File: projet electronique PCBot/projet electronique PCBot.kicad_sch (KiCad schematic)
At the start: 0 parts

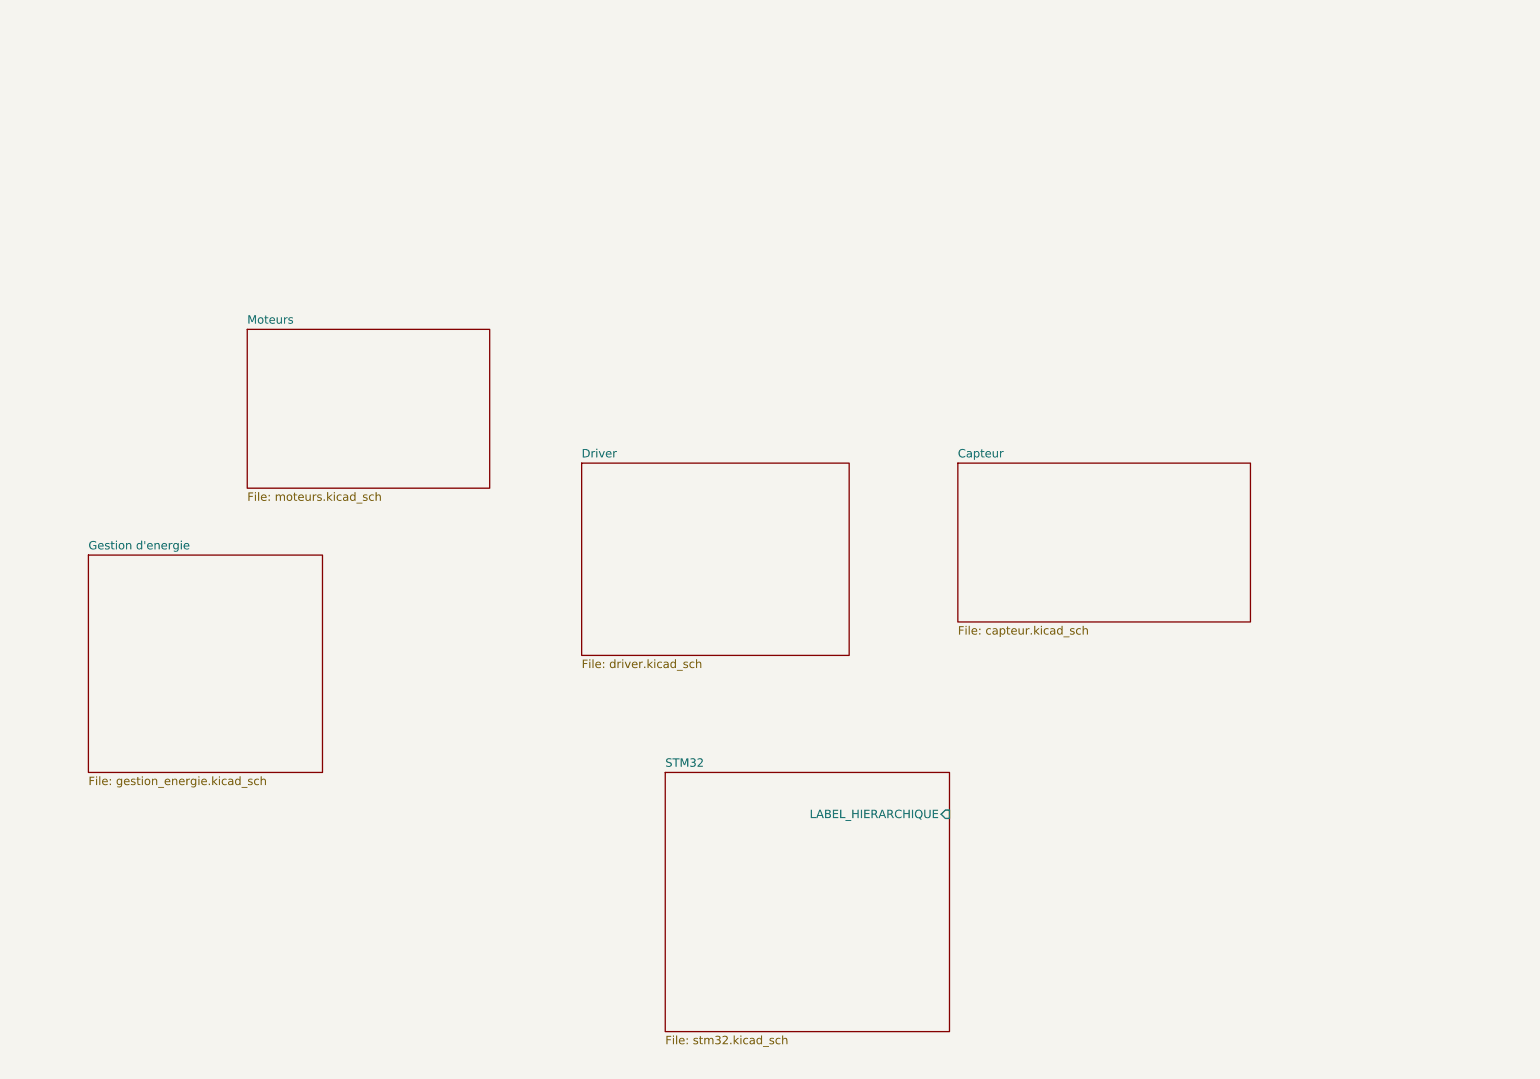
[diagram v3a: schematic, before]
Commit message: Modification des feuilles hiérarchiques et le main
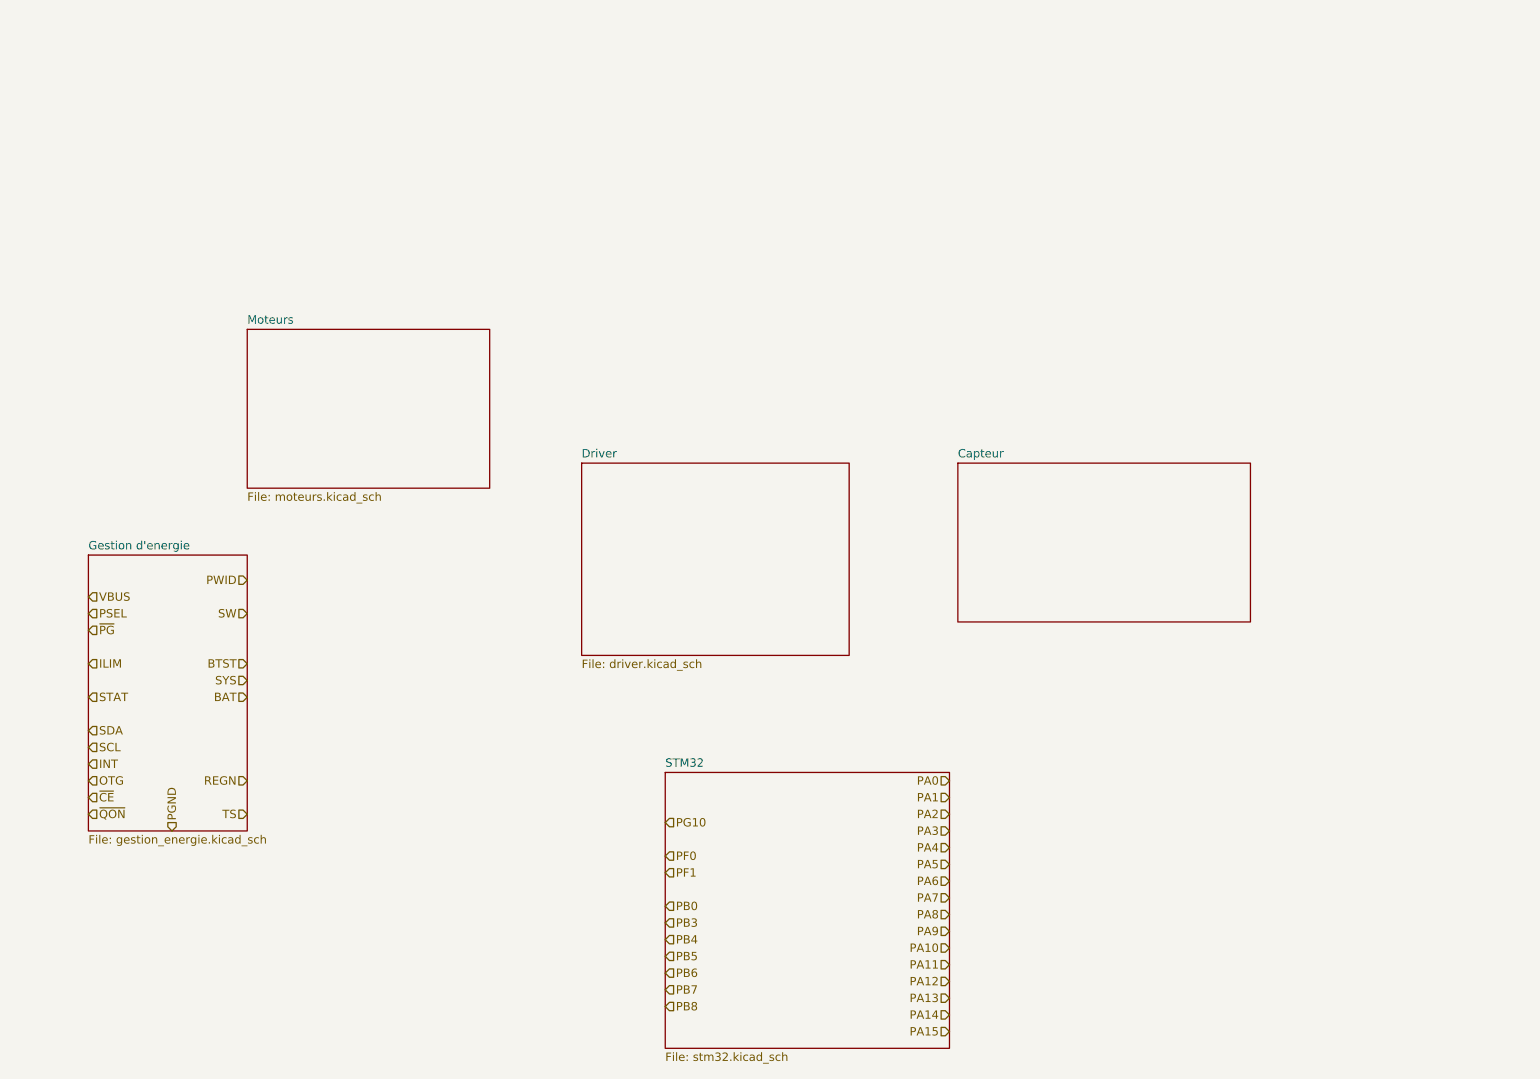
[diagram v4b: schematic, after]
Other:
- sheet STM32 ports: added none; removed LABEL_HIERARCHIQUE
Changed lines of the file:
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@@
     (comment 4 "Sara KABBANI")
   )
-  (sheet (at 115.57 137.16) (size 43.18 39.37) (fields_autoplaced)
+  (hierarchical_label "PF1" (shape input) (at 115.57 152.4 0) (fields_autoplaced)
+    (effects (font (size 1.27 1.27)) (justify left))
+  )
+  (hierarchical_label "PA6" (shape input) (at 158.75 153.67 180) (fields_autoplaced)
+    (effects (font (size 1.27 1.27)) (justify right))
+  )
+  (hierarchical_label "PA8" (shape input) (at 158.75 158.75 180) (fields_autoplaced)
+    (effects (font (size 1.27 1.27)) (justify right))
+  )
+  (hierarchical_label "PA10" (shape input) (at 158.75 163.83 180) (fields_autoplaced)
+    (effects (font (size 1.27 1.27)) (justify right))
+  )
+  (hierarchical_label "TS" (shape input) (at 52.07 143.51 180) (fields_autoplaced)
+    (effects (font (size 1.27 1.27)) (justify right))
+  )
+  (hierarchical_label "OTG" (shape input) (at 27.94 138.43 0) (fields_autoplaced)
+    (effects (font (size 1.27 1.27)) (justify left))
+  )
+  (hierarchical_label "SCL" (shape input) (at 27.94 133.35 0) (fields_autoplaced)
+    (effects (font (size 1.27 1.27)) (justify left))
+  )
+  (hierarchical_label "SDA" (shape input) (at 27.94 130.81 0) (fields_autoplaced)
+    (effects (font (size 1.27 1.27)) (justify left))
+  )
+  (hierarchical_label "STAT" (shape input) (at 27.94 125.73 0) (fields_autoplaced)
+    (effects (font (size 1.27 1.27)) (justify left))
+  )
+  (hierarchical_label "~{CE}" (shape input) (at 27.94 140.97 0) (fields_autoplaced)
+    (effects (font (size 1.27 1.27)) (justify left))
+  )
+  (hierarchical_label "PB3" (shape input) (at 115.57 160.02 0) (fields_autoplaced)
+    (effects (font (size 1.27 1.27)) (justify left))
+  )
+  (hierarchical_label "PA13" (shape input) (at 158.75 171.45 180) (fields_autoplaced)
+    (effects (font (size 1.27 1.27)) (justify right))
+  )
+  (hierarchical_label "PA3" (shape input) (at 158.75 146.05 180) (fields_autoplaced)
+    (effects (font (size 1.27 1.27)) (justify right))
+  )
+  (hierarchical_label "PB8" (shape input) (at 115.57 172.72 0) (fields_autoplaced)
+    (effects (font (size 1.27 1.27)) (justify left))
+  )
+  (hierarchical_label "PA4" (shape input) (at 158.75 148.59 180) (fields_autoplaced)
+    (effects (font (size 1.27 1.27)) (justify right))
+  )
+  (hierarchical_label "~{QON}" (shape input) (at 27.94 143.51 0) (fields_autoplaced)
+    (effects (font (size 1.27 1.27)) (justify left))
+  )
+  (hierarchical_label "PA0" (shape input) (at 158.75 138.43 180) (fields_autoplaced)
+    (effects (font (size 1.27 1.27)) (justify right))
+  )
+  (hierarchical_label "PB6" (shape input) (at 115.57 167.64 0) (fields_autoplaced)
+    (effects (font (size 1.27 1.27)) (justify left))
+  )
+  (hierarchical_label "PB0" (shape input) (at 115.57 157.48 0) (fields_autoplaced)
+    (effects (font (size 1.27 1.27)) (justify left))
+  )
+  (hierarchical_label "PGND" (shape input) (at 40.64 146.05 90) (fields_autoplaced)
+    (effects (font (size 1.27 1.27)) (justify left))
+  )
+  (hierarchical_label "INT" (shape input) (at 27.94 135.89 0) (fields_autoplaced)
+    (effects (font (size 1.27 1.27)) (justify left))
+  )
+  (hierarchical_label "PG10" (shape input) (at 115.57 144.78 0) (fields_autoplaced)
+    (effects (font (size 1.27 1.27)) (justify left))
+  )
+  (hierarchical_label "SW" (shape input) (at 52.07 113.03 180) (fields_autoplaced)
+    (effects (font (size 1.27 1.27)) (justify right))
+  )
+  (hierarchical_label "PA9" (shape input) (at 158.75 161.29 180) (fields_autoplaced)
+    (effects (font (size 1.27 1.27)) (justify right))
+  )
+  (hierarchical_label "~{PG}" (shape input) (at 27.94 115.57 0) (fields_autoplaced)
+    (effects (font (size 1.27 1.27)) (justify left))
+  )
+  (hierarchical_label "BAT" (shape input) (at 52.07 125.73 180) (fields_autoplaced)
+    (effects (font (size 1.27 1.27)) (justify right))
+  )
+  (hierarchical_label "PA12" (shape input) (at 158.75 168.91 180) (fields_autoplaced)
+    (effects (font (size 1.27 1.27)) (justify right))
+  )
+  (hierarchical_label "REGN" (shape input) (at 52.07 138.43 180) (fields_autoplaced)
+    (effects (font (size 1.27 1.27)) (justify right))
+  )
+  (hierarchical_label "BTST" (shape input) (at 52.07 120.65 180) (fields_autoplaced)
+    (effects (font (size 1.27 1.27)) (justify right))
+  )
+  (hierarchical_label "PA5" (shape input) (at 158.75 151.13 180) (fields_autoplaced)
+    (effects (font (size 1.27 1.27)) (justify right))
+  )
+  (hierarchical_label "PWID" (shape input) (at 52.07 107.95 180) (fields_autoplaced)
+    (effects (font (size 1.27 1.27)) (justify right))
+  )
+  (hierarchical_label "PA15" (shape input) (at 158.75 176.53 180) (fields_autoplaced)
+    (effects (font (size 1.27 1.27)) (justify right))
+  )
+  (hierarchical_label "PSEL" (shape input) (at 27.94 113.03 0) (fields_autoplaced)
+    (effects (font (size 1.27 1.27)) (justify left))
+  )
+  (hierarchical_label "PA1" (shape input) (at 158.75 140.97 180) (fields_autoplaced)
+    (effects (font (size 1.27 1.27)) (justify right))
+  )
+  (hierarchical_label "PA14" (shape input) (at 158.75 173.99 180) (fields_autoplaced)
+    (effects (font (size 1.27 1.27)) (justify right))
+  )
+  (hierarchical_label "PB4" (shape input) (at 115.57 162.56 0) (fields_autoplaced)
+    (effects (font (size 1.27 1.27)) (justify left))
+  )
+  (hierarchical_label "PA7" (shape input) (at 158.75 156.21 180) (fields_autoplaced)
+    (effects (font (size 1.27 1.27)) (justify right))
+  )
+  (hierarchical_label "PF0" (shape input) (at 115.57 149.86 0) (fields_autoplaced)
+    (effects (font (size 1.27 1.27)) (justify left))
+  )
+  (hierarchical_label "ILIM" (shape input) (at 27.94 120.65 0) (fields_autoplaced)
+    (effects (font (size 1.27 1.27)) (justify left))
+  )
+  (hierarchical_label "PB7" (shape input) (at 115.57 170.18 0) (fields_autoplaced)
+    (effects (font (size 1.27 1.27)) (justify left))
+  )
+  (hierarchical_label "PB5" (shape input) (at 115.57 165.1 0) (fields_autoplaced)
+    (effects (font (size 1.27 1.27)) (justify left))
+  )
+  (hierarchical_label "PA11" (shape input) (at 158.75 166.37 180) (fields_autoplaced)
+    (effects (font (size 1.27 1.27)) (justify right))
+  )
+  (hierarchical_label "SYS" (shape input) (at 52.07 123.19 180) (fields_autoplaced)
+    (effects (font (size 1.27 1.27)) (justify right))
+  )
+  (hierarchical_label "VBUS" (shape input) (at 27.94 110.49 0) (fields_autoplaced)
+    (effects (font (size 1.27 1.27)) (justify left))
+  )
+  (hierarchical_label "PA2" (shape input) (at 158.75 143.51 180) (fields_autoplaced)
+    (effects (font (size 1.27 1.27)) (justify right))
+  )
+  (sheet (at 115.57 137.16) (size 43.18 41.91) (fields_autoplaced)
     (stroke (width 0.1524) (type solid))
     (fill (color 0 0 0 0.0000))
@@
       (effects (font (size 1.27 1.27)) (justify left bottom))
     )
-    (property "Sheetfile" "stm32.kicad_sch" (at 115.57 177.1146 0)
-      (effects (font (size 1.27 1.27)) (justify left top))
-    )
-    (pin "LABEL_HIERARCHIQUE" input (at 158.75 143.51 0)
-      (effects (font (size 1.27 1.27)) (justify right))
+    (property "Sheetfile" "stm32.kicad_sch" (at 115.57 179.6546 0)
+      (effects (font (size 1.27 1.27)) (justify left top))
     )
     (instances
@@
     )
     (property "Sheetfile" "capteur.kicad_sch" (at 160.02 114.8846 0)
-      (effects (font (size 1.27 1.27)) (justify left top))
+      (effects (font (size 1.27 1.27)) (justify left top) hide)
     )
     (instances
@@
     )
   )
-  (sheet (at 27.94 104.14) (size 35.56 33.02) (fields_autoplaced)
+  (sheet (at 27.94 104.14) (size 24.13 41.91) (fields_autoplaced)
     (stroke (width 0.1524) (type solid))
     (fill (color 0 0 0 0.0000))
@@
       (effects (font (size 1.27 1.27)) (justify left bottom))
     )
-    (property "Sheetfile" "gestion_energie.kicad_sch" (at 27.94 137.7446 0)
-      (effects (font (size 1.27 1.27)) (justify left top))
-    )
+    (property "Sheetfile" "gestion_energie.kicad_sch" (at 27.94 146.6346 0)
+      (effects (font (size 1.27 1.27)) (justify left top))
+    )

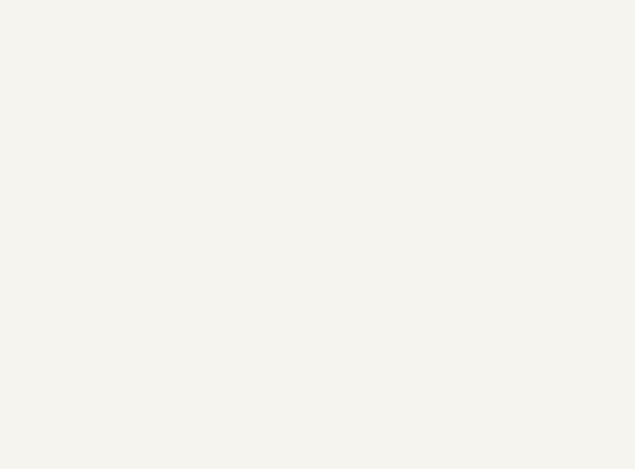
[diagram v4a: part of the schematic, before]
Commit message: ajout de la feuille connecteurs
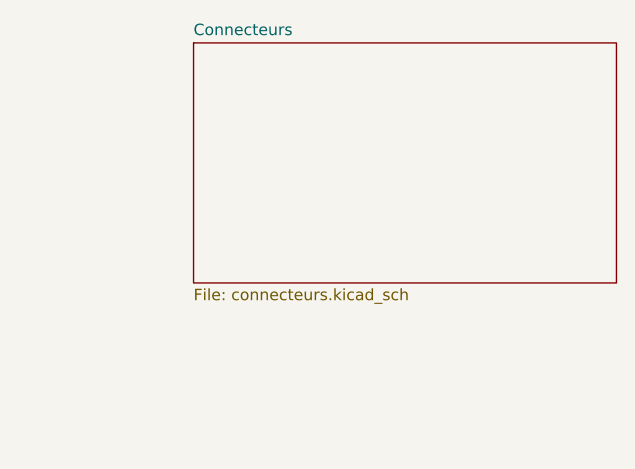
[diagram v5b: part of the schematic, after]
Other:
- added sheet Connecteurs (connecteurs.kicad_sch)

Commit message: ajout de la feuille usb
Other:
- added sheet USB (usb.kicad_sch)
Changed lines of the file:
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@@
+		)
+	)
+	(sheet
+		(at 87.63 27.94)
+		(size 40.64 22.86)
+		(exclude_from_sim no)
+		(in_bom yes)
+		(on_board yes)
+		(dnp no)
+		(fields_autoplaced yes)
+		(stroke
+			(width 0.1524)
+			(type solid)
+		)
+		(fill
+			(color 0 0 0 0.0000)
+		)
+		(property "Sheetname" "USB"
+			(at 87.63 27.2284 0)
+			(effects
+				(font
+					(size 1.27 1.27)
+				)
+				(justify left bottom)
+			)
+		)
+		(property "Sheetfile" "usb.kicad_sch"
+			(at 87.63 51.3846 0)
+			(effects
+				(font
+					(size 1.27 1.27)
+				)
+				(justify left top)
+			)
+		)
+		(instances
+			(project "projet electronique PCBot"
+				(path "/210be09d-86cd-4faa-bb91-cc54c5972517"
+					(page "8")
+				)
+			)
 		)
 	)

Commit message: Ajour USB
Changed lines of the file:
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@@
 		(comment 4 "Sara KABBANI")
 	)
+	(wire
+		(pts
+			(xy 52.07 129.54) (xy 69.85 129.54)
+		)
+		(stroke
+			(width 0)
+			(type default)
+		)
+	)
 	(hierarchical_label "PF1"
 		(shape input)
@@
 		)
 	)
+	(hierarchical_label "VBUS"
+		(shape input)
+		(at 52.07 129.54 180)
+		(effects
+			(font
+				(size 1.27 1.27)
+			)
+			(justify right)
+		)
+	)
 	(hierarchical_label "TS"
 		(shape input)
-		(at 52.07 143.51 180)
+		(at 93.98 162.56 180)
 		(effects
 			(font
@@
 	(hierarchical_label "OTG"
 		(shape input)
-		(at 27.94 138.43 0)
+		(at 69.85 157.48 0)
 		(effects
 			(font
@@
 	(hierarchical_label "SCL"
 		(shape input)
-		(at 27.94 133.35 0)
-		(effects
-			(font
-				(size 1.27 1.27)
-			)
-			(justify left)
+		(at 69.85 152.4 0)
+		(effects
+			(font
+				(size 1.27 1.27)
+			)
+			(justify left)
+		)
+	)
+	(hierarchical_label "D-"
+		(shape input)
+		(at 52.07 137.16 180)
+		(effects
+			(font
+				(size 1.27 1.27)
+			)
+			(justify right)
 		)
 	)
 	(hierarchical_label "SDA"
 		(shape input)
-		(at 27.94 130.81 0)
+		(at 69.85 149.86 0)
 		(effects
 			(font
@@
 	(hierarchical_label "STAT"
 		(shape input)
-		(at 27.94 125.73 0)
+		(at 69.85 144.78 0)
 		(effects
 			(font
@@
 	(hierarchical_label "~{CE}"
 		(shape input)
-		(at 27.94 140.97 0)
+		(at 69.85 160.02 0)
 		(effects
 			(font
@@
 	(hierarchical_label "~{QON}"
 		(shape input)
-		(at 27.94 143.51 0)
+		(at 69.85 162.56 0)
 		(effects
 			(font
@@
 	(hierarchical_label "PGND"
 		(shape input)
-		(at 40.64 146.05 90)
+		(at 82.55 165.1 90)
 		(effects
 			(font
@@
 	(hierarchical_label "INT"
 		(shape input)
-		(at 27.94 135.89 0)
+		(at 69.85 154.94 0)
 		(effects
 			(font
@@
 	(hierarchical_label "SW"
 		(shape input)
-		(at 52.07 113.03 180)
+		(at 93.98 132.08 180)
+		(effects
+			(font
+				(size 1.27 1.27)
+			)
+			(justify right)
+		)
+	)
+	(hierarchical_label "D+"
+		(shape input)
+		(at 52.07 134.62 180)
 		(effects
 			(font
@@
 	(hierarchical_label "~{PG}"
 		(shape input)
-		(at 27.94 115.57 0)
+		(at 69.85 134.62 0)
 		(effects
 			(font
@@
 	(hierarchical_label "BAT"
 		(shape input)
-		(at 52.07 125.73 180)
+		(at 93.98 144.78 180)
 		(effects
 			(font
@@
 	(hierarchical_label "REGN"
 		(shape input)
-		(at 52.07 138.43 180)
+		(at 93.98 157.48 180)
 		(effects
 			(font
@@
 	(hierarchical_label "BTST"
 		(shape input)
-		(at 52.07 120.65 180)
+		(at 93.98 139.7 180)
 		(effects
 			(font
@@
 	(hierarchical_label "PWID"
 		(shape input)
-		(at 52.07 107.95 180)
+		(at 93.98 127 180)
 		(effects
 			(font
@@
 	(hierarchical_label "PSEL"
 		(shape input)
-		(at 27.94 113.03 0)
+		(at 69.85 132.08 0)
 		(effects
 			(font
@@
 	(hierarchical_label "ILIM"
 		(shape input)
-		(at 27.94 120.65 0)
+		(at 69.85 139.7 0)
 		(effects
 			(font
@@
 	(hierarchical_label "SYS"
 		(shape input)
-		(at 52.07 123.19 180)
+		(at 93.98 142.24 180)
 		(effects
 			(font
@@
 	(hierarchical_label "VBUS"
 		(shape input)
-		(at 27.94 110.49 0)
+		(at 69.85 129.54 0)
 		(effects
 			(font
@@
 				)
 				(justify left top)
-				(hide yes)
 			)
 		)
@@
 	)
 	(sheet
-		(at 27.94 104.14)
+		(at 69.85 123.19)
 		(size 24.13 41.91)
 		(exclude_from_sim no)
@@
 		)
 		(property "Sheetname" "Gestion d'energie"
-			(at 27.94 103.4284 0)
+			(at 69.85 122.4784 0)
 			(effects
 				(font
@@
 		)
 		(property "Sheetfile" "gestion_energie.kicad_sch"
-			(at 27.94 146.6346 0)
+			(at 69.85 165.6846 0)
 			(effects
 				(font
@@
 	)
 	(sheet
-		(at 87.63 27.94)
-		(size 40.64 22.86)
+		(at 39.37 124.46)
+		(size 12.7 22.86)
 		(exclude_from_sim no)
 		(in_bom yes)
@@
 		)
 		(property "Sheetname" "USB"
-			(at 87.63 27.2284 0)
+			(at 39.37 123.7484 0)
 			(effects
 				(font
@@
 		)
 		(property "Sheetfile" "usb.kicad_sch"
-			(at 87.63 51.3846 0)
-			(effects
-				(font
+			(at 39.37 147.9046 0)
+			(effects
+				(font

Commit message: feuille driver 2
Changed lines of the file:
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@@
+		)
+	)
+	(hierarchical_label "PA3"
+		(shape input)
+		(at 102.87 114.3 0)
+		(effects
+			(font
+				(size 1.27 1.27)
+			)
+			(justify left)
 		)
 	)
@@
 		)
 	)
+	(hierarchical_label "PA1"
+		(shape input)
+		(at 102.87 109.22 0)
+		(effects
+			(font
+				(size 1.27 1.27)
+			)
+			(justify left)
+		)
+	)
+	(hierarchical_label "PA2"
+		(shape input)
+		(at 102.87 111.76 0)
+		(effects
+			(font
+				(size 1.27 1.27)
+			)
+			(justify left)
+		)
+	)
 	(hierarchical_label "~{QON}"
 		(shape input)
@@
 		)
 	)
+	(hierarchical_label "SYS"
+		(shape input)
+		(at 137.16 90.17 270)
+		(effects
+			(font
+				(size 1.27 1.27)
+			)
+			(justify right)
+		)
+	)
 	(hierarchical_label "PA9"
 		(shape input)
@@
 		)
 	)
+	(hierarchical_label "PA0"
+		(shape input)
+		(at 102.87 106.68 0)
+		(effects
+			(font
+				(size 1.27 1.27)
+			)
+			(justify left)
+		)
+	)
 	(hierarchical_label "PF0"
 		(shape input)
@@
 		(effects
 			(font
+				(size 1.27 1.27)
+			)
+			(justify right)
+		)
+	)
+	(hierarchical_label "PA0"
+		(shape input)
+		(at 129.54 90.17 270)
+		(effects
+			(font
